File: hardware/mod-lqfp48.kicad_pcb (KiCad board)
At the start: 2 copper layers, 23.4 x 12.7 mm, 9 parts, among them J1 Target, U1 STM32F103C8Tx, Y1 8MHz

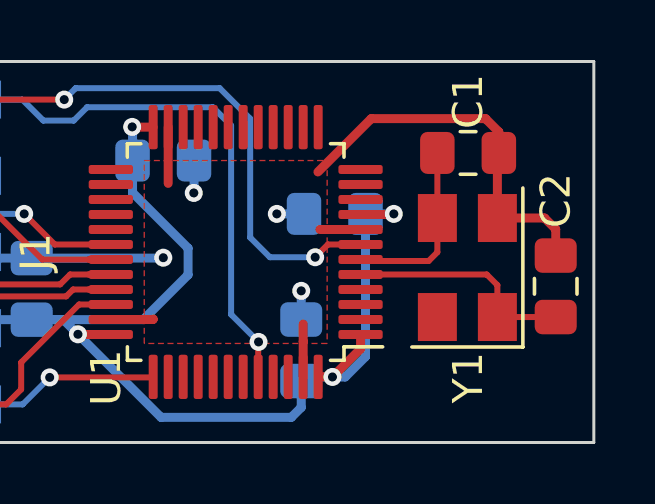
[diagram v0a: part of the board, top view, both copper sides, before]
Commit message: Fix DRC warnings in mod-lqfp48
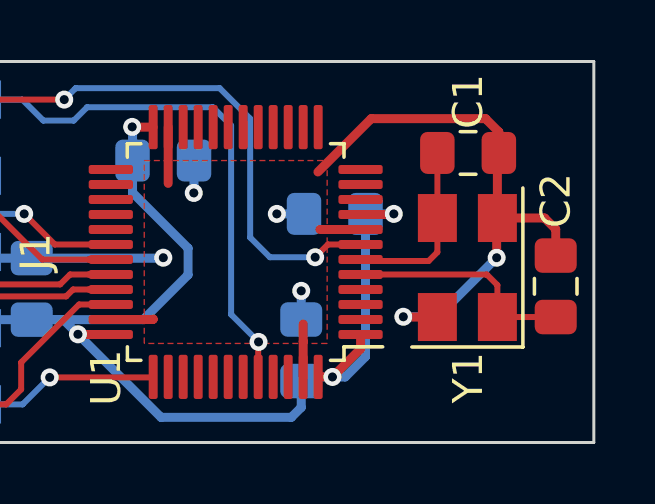
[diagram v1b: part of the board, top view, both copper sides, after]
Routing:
- net GND: track 29.8 -> 36.2 mm, vias 4 -> 6
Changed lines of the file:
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@@
     (thickness 1.5)
     (drawings 4)
-    (tracks 134)
+    (tracks 142)
     (zones 0)
     (modules 9)
@@
   (segment (start 99.197 95.387) (end 97.623 95.387) (width 0.3) (layer F.Cu) (net 1))
   (segment (start 99.568 95.758) (end 99.197 95.387) (width 0.3) (layer F.Cu) (net 1))
+  (via (at 97.5995 96.7105) (size 0.6) (drill 0.3) (layers F.Cu B.Cu) (net 1))
+  (segment (start 97.5995 95.4105) (end 97.623 95.387) (width 0.3) (layer F.Cu) (net 1))
+  (segment (start 97.5995 96.7105) (end 97.5995 95.4105) (width 0.3) (layer F.Cu) (net 1))
+  (segment (start 95.631 98.679) (end 94.488 98.679) (width 0.3) (layer B.Cu) (net 1))
+  (segment (start 97.5995 96.7105) (end 95.631 98.679) (width 0.3) (layer B.Cu) (net 1))
+  (segment (start 95.623 98.687) (end 94.496 98.687) (width 0.3) (layer F.Cu) (net 1))
+  (via (at 94.488 98.679) (size 0.6) (drill 0.3) (layers F.Cu B.Cu) (net 1))
+  (segment (start 94.496 98.687) (end 94.488 98.679) (width 0.3) (layer F.Cu) (net 1))
   (via (at 91.549021 96.694545) (size 0.6) (drill 0.3) (layers F.Cu B.Cu) (net 2))
   (segment (start 93.0625 96.27) (end 91.973566 96.27) (width 0.2) (layer F.Cu) (net 2))

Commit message: Use Rezonit solder mask parameters
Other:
- rule pad_to_mask_clearance: 0 -> 0.05
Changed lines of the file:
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@@
     (pad_size 1.524 1.524)
     (pad_drill 0.762)
-    (pad_to_mask_clearance 0)
+    (pad_to_mask_clearance 0.05)
+    (solder_mask_min_width 0.15)
     (aux_axis_origin 0 0)
     (visible_elements FFFDFF7F)
@@
       (viasonmask false)
       (mode 1)
-      (useauxorigin false)
+      (useauxorigin true)
       (hpglpennumber 1)
       (hpglpenspeed 20)
@@
       (outputformat 1)
       (mirror false)
-      (drillshape 1)
+      (drillshape 0)
       (scaleselection 1)
-      (outputdirectory ""))
+      (outputdirectory "out48"))
   )
   (net 0 "")

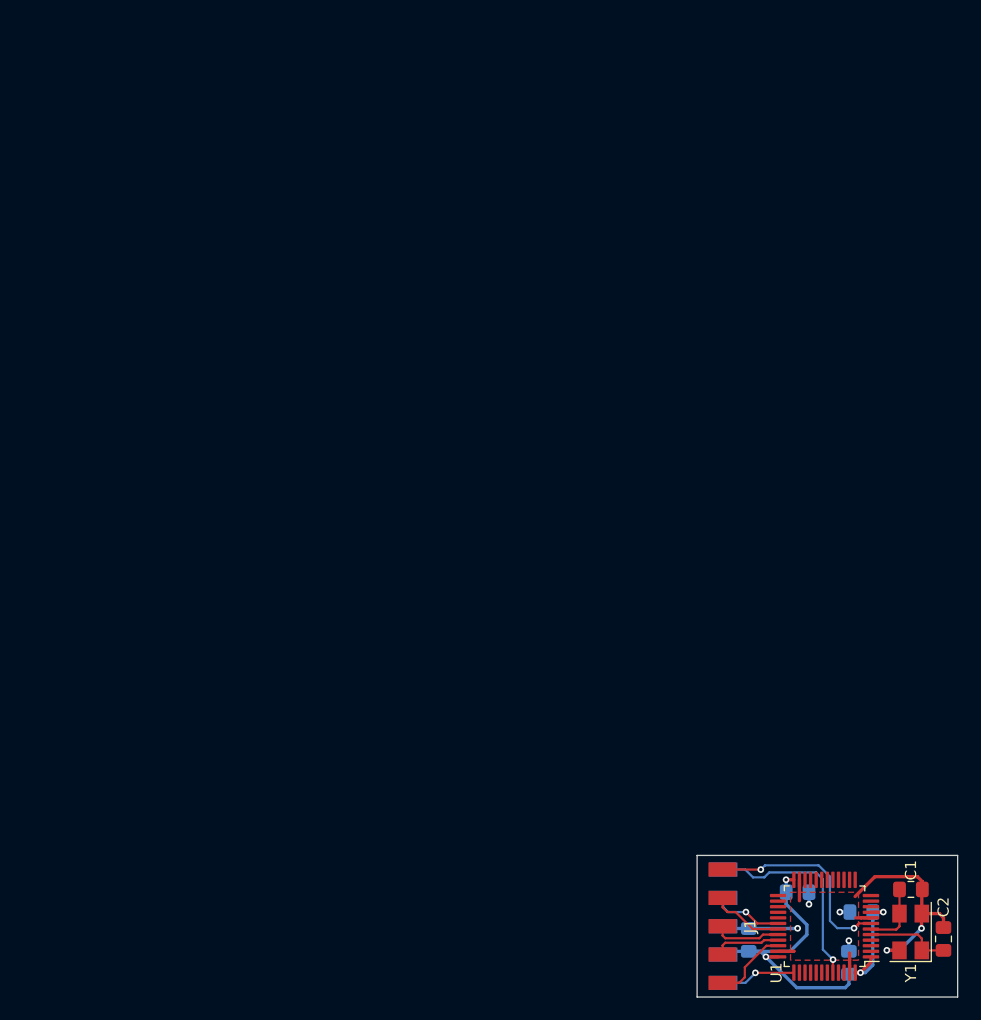
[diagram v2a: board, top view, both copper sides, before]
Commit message: Align boards to the 1mm grid
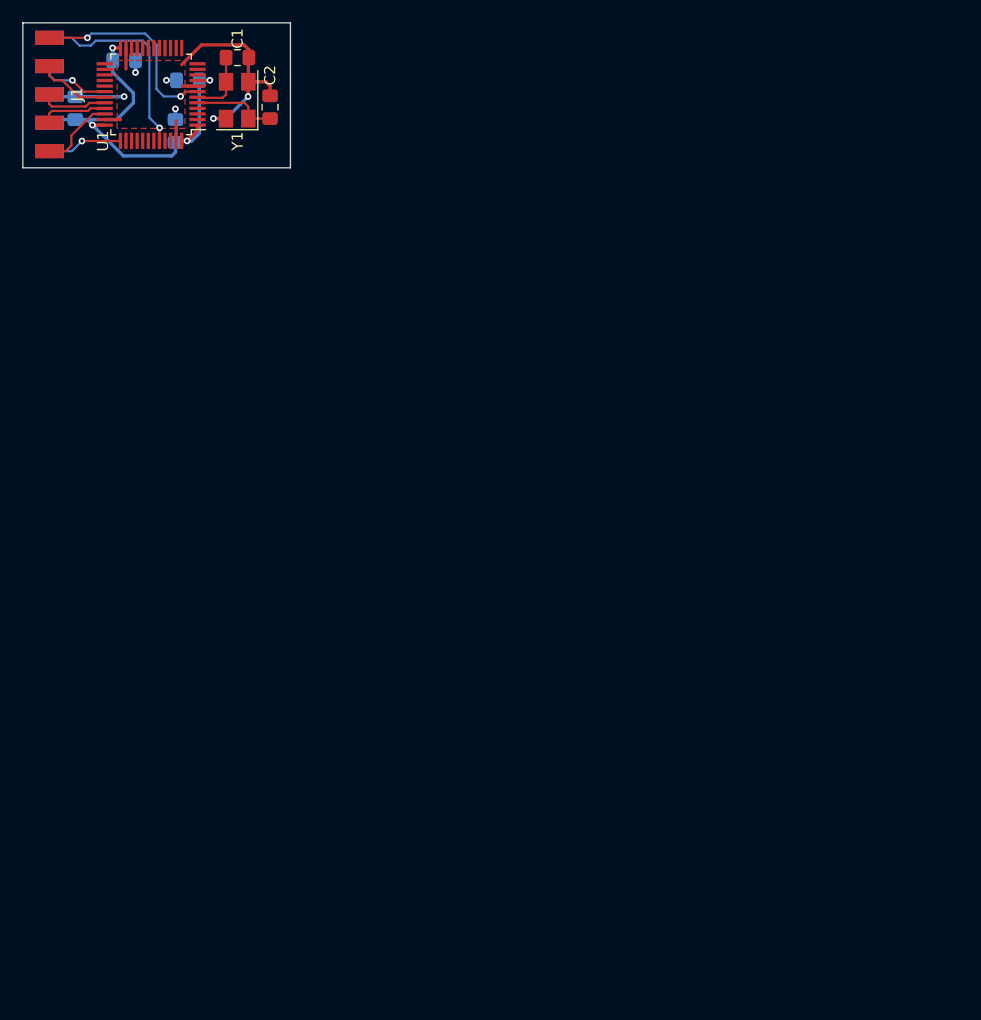
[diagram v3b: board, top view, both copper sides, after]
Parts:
- moved C1 96.0 mm to (36.2, 18.6)
- moved Y1 96.0 mm to (36.2, 22.4)
- moved C2 96.0 mm to (39.2, 23.1)
- moved C3 96.0 mm to (31.8, 20.6)
- moved C4 96.0 mm to (30.7, 25.2)
- moved C5 96.0 mm to (26.1, 18.9)
- moved C6 96.0 mm to (21.7, 23.1)
- moved J1 96.0 mm to (19.4, 21.9)
- moved U1 96.0 mm to (28.5, 21.9)
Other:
- board size 23.4 x 12.7 mm -> 24 x 13 mm

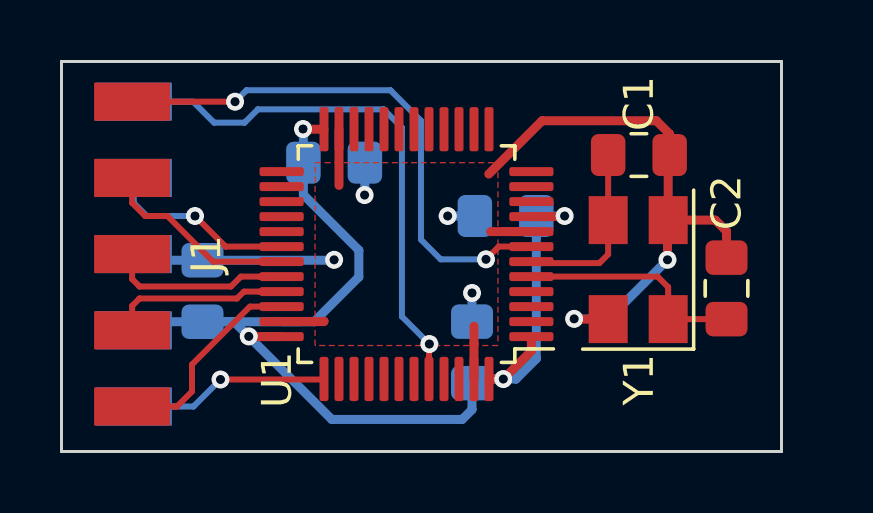
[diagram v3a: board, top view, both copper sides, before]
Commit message: Resize the mod-lqfp48 board
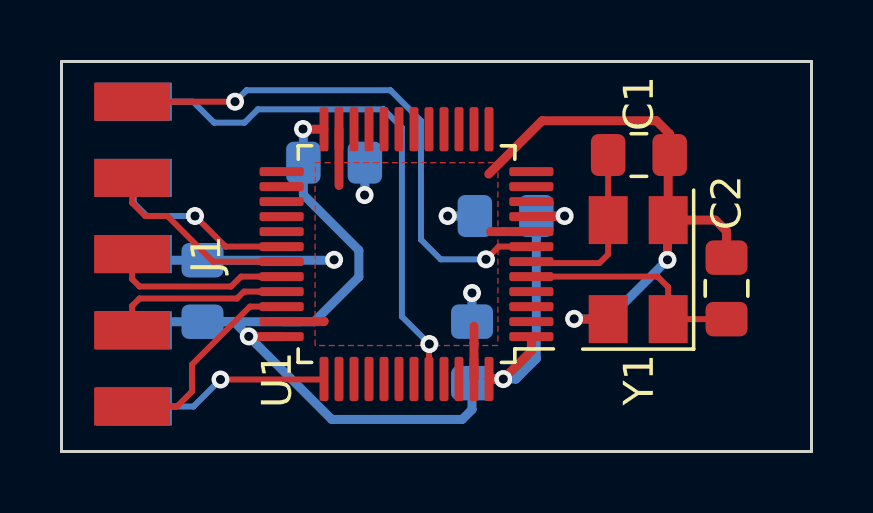
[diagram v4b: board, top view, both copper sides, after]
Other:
- board size 24 x 13 mm -> 25 x 13 mm
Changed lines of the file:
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@@
   )
   (gr_line (start 17 15.5) (end 17 28.5) (layer Edge.Cuts) (width 0.1))
-  (gr_line (start 41 28.5) (end 41 15.5) (layer Edge.Cuts) (width 0.1))
-  (gr_line (start 17 28.5) (end 41 28.5) (layer Edge.Cuts) (width 0.1))
-  (gr_line (start 17 15.5) (end 41 15.5) (layer Edge.Cuts) (width 0.1))
+  (gr_line (start 42 28.5) (end 42 15.5) (layer Edge.Cuts) (width 0.1))
+  (gr_line (start 17 28.5) (end 42 28.5) (layer Edge.Cuts) (width 0.1))
+  (gr_line (start 17 15.5) (end 42 15.5) (layer Edge.Cuts) (width 0.1))
   (segment (start 30.75 24.9) (end 30.75 26.0825) (width 0.3) (layer F.Cu) (net 1))
   (segment (start 19.408948 21.92) (end 19.97 21.92) (width 0.3) (layer B.Cu) (net 1))
